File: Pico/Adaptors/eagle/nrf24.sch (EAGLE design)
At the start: 3 parts

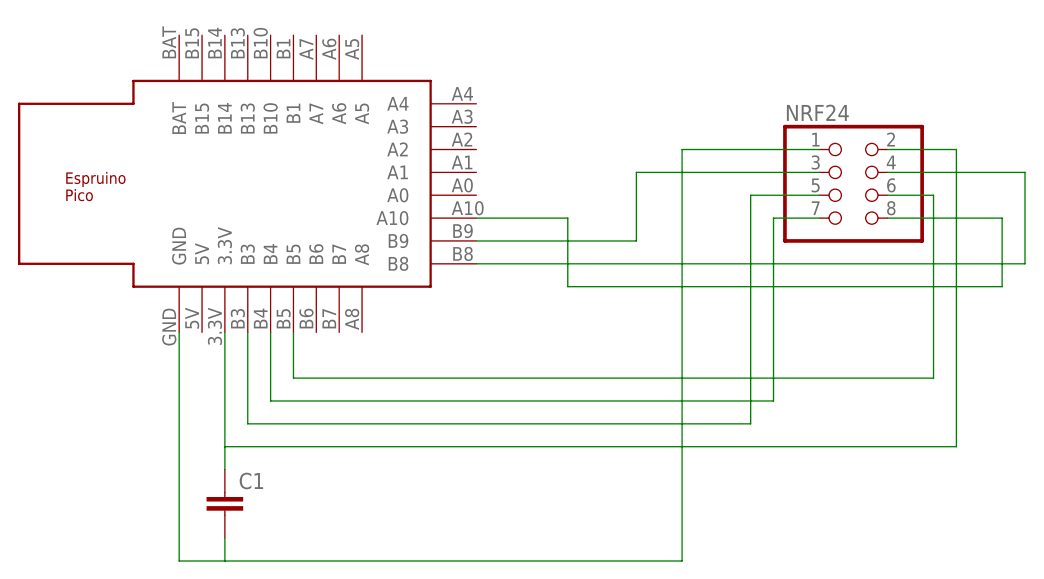
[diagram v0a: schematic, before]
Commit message: updated NRF24, new Pico library part that does 0.1 holes and 0.05 SMD
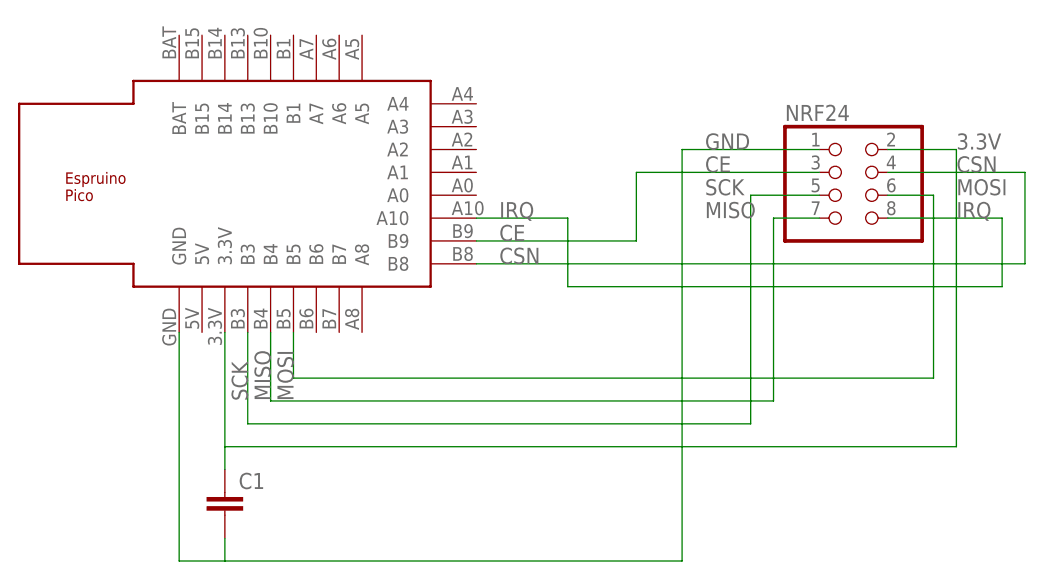
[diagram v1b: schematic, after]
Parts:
- removed U$1: ESPRUINO_PICO_SMDONLY, espruino_pico:ESPRUINO_PICO_SMDONLY
- added U$2: ESPRUINO_PICO_HALFSMD, espruino_pico:ESPRUINO_PICO_HALFSMD
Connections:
- removed net N$1: C1.1, NRF24.2, U$1.3.3V
- removed net N$2: C1.2, NRF24.1, U$1.GND
- removed net N$4: NRF24.5, U$1.B3
- removed net N$5: NRF24.7, U$1.B4
- removed net N$6: NRF24.6, U$1.B5
- removed net N$7: NRF24.4, U$1.B8
- removed net N$8: NRF24.3, U$1.B9
- removed net N$9: NRF24.8, U$1.A10
- new net 3.3V: C1.1, NRF24.2, U$2.3.3V
- new net CE: NRF24.3, U$2.B9
- new net CSN: NRF24.4, U$2.B8
- new net GND: C1.2, NRF24.1, U$2.GND
- new net IRQ: NRF24.8, U$2.A10
- new net MISO: NRF24.7, U$2.B4
- new net MOSI: NRF24.6, U$2.B5
- new net SCK: NRF24.5, U$2.B3
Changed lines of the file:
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@@
 <grid distance="0.1" unitdist="inch" unit="inch" style="lines" multiple="1" display="no" altdistance="0.01" altunitdist="inch" altunit="inch"/>
 <layers>
-<layer number="1" name="Top" color="4" fill="1" visible="no" active="no"/>
-<layer number="16" name="Bottom" color="1" fill="1" visible="no" active="no"/>
-<layer number="17" name="Pads" color="2" fill="1" visible="no" active="no"/>
-<layer number="18" name="Vias" color="2" fill="1" visible="no" active="no"/>
-<layer number="19" name="Unrouted" color="6" fill="1" visible="no" active="no"/>
-<layer number="20" name="Dimension" color="15" fill="1" visible="no" active="no"/>
-<layer number="21" name="tPlace" color="7" fill="1" visible="no" active="no"/>
-<layer number="22" name="bPlace" color="7" fill="1" visible="no" active="no"/>
-<layer number="23" name="tOrigins" color="15" fill="1" visible="no" active="no"/>
-<layer number="24" name="bOrigins" color="15" fill="1" visible="no" active="no"/>
-<layer number="25" name="tNames" color="7" fill="1" visible="no" active="no"/>
-<layer number="26" name="bNames" color="7" fill="1" visible="no" active="no"/>
-<layer number="27" name="tValues" color="7" fill="1" visible="no" active="no"/>
-<layer number="28" name="bValues" color="7" fill="1" visible="no" active="no"/>
+<layer number="1" name="Top" color="4" fill="1" visible="yes" active="no"/>
+<layer number="16" name="Bottom" color="1" fill="1" visible="yes" active="no"/>
+<layer number="17" name="Pads" color="2" fill="1" visible="yes" active="no"/>
+<layer number="18" name="Vias" color="2" fill="1" visible="yes" active="no"/>
+<layer number="19" name="Unrouted" color="6" fill="1" visible="yes" active="no"/>
+<layer number="20" name="Dimension" color="15" fill="1" visible="yes" active="no"/>
+<layer number="21" name="tPlace" color="7" fill="1" visible="yes" active="no"/>
+<layer number="22" name="bPlace" color="7" fill="1" visible="yes" active="no"/>
+<layer number="23" name="tOrigins" color="15" fill="1" visible="yes" active="no"/>
+<layer number="24" name="bOrigins" color="15" fill="1" visible="yes" active="no"/>
+<layer number="25" name="tNames" color="7" fill="1" visible="yes" active="no"/>
+<layer number="26" name="bNames" color="7" fill="1" visible="yes" active="no"/>
+<layer number="27" name="tValues" color="7" fill="1" visible="yes" active="no"/>
+<layer number="28" name="bValues" color="7" fill="1" visible="yes" active="no"/>
 <layer number="29" name="tStop" color="7" fill="3" visible="no" active="no"/>
 <layer number="30" name="bStop" color="7" fill="6" visible="no" active="no"/>
@@
 <layer number="35" name="tGlue" color="7" fill="4" visible="no" active="no"/>
 <layer number="36" name="bGlue" color="7" fill="5" visible="no" active="no"/>
-<layer number="37" name="tTest" color="7" fill="1" visible="no" active="no"/>
-<layer number="38" name="bTest" color="7" fill="1" visible="no" active="no"/>
+<layer number="37" name="tTest" color="7" fill="1" visible="yes" active="no"/>
+<layer number="38" name="bTest" color="7" fill="1" visible="yes" active="no"/>
 <layer number="39" name="tKeepout" color="4" fill="11" visible="no" active="no"/>
 <layer number="40" name="bKeepout" color="1" fill="11" visible="no" active="no"/>
@@
 <layer number="44" name="Drills" color="7" fill="1" visible="no" active="no"/>
 <layer number="45" name="Holes" color="7" fill="1" visible="no" active="no"/>
-<layer number="46" name="Milling" color="3" fill="1" visible="no" active="no"/>
-<layer number="47" name="Measures" color="7" fill="1" visible="no" active="no"/>
-<layer number="48" name="Document" color="7" fill="1" visible="no" active="no"/>
-<layer number="49" name="Reference" color="7" fill="1" visible="no" active="no"/>
-<layer number="51" name="tDocu" color="7" fill="1" visible="no" active="no"/>
-<layer number="52" name="bDocu" color="7" fill="1" visible="no" active="no"/>
+<layer number="46" name="Milling" color="3" fill="1" visible="yes" active="no"/>
+<layer number="47" name="Measures" color="7" fill="1" visible="yes" active="no"/>
+<layer number="48" name="Document" color="7" fill="1" visible="yes" active="no"/>
+<layer number="49" name="Reference" color="7" fill="1" visible="yes" active="no"/>
+<layer number="51" name="tDocu" color="7" fill="1" visible="yes" active="no"/>
+<layer number="52" name="bDocu" color="7" fill="1" visible="yes" active="no"/>
 <layer number="91" name="Nets" color="2" fill="1" visible="yes" active="yes"/>
 <layer number="92" name="Busses" color="1" fill="1" visible="yes" active="yes"/>
@@
 <part name="NRF24" library="pinhead" deviceset="PINHD-2X4" device=""/>
 <part name="C1" library="rcl" deviceset="C-EU" device="C1206"/>
-<part name="U$1" library="espruino_pico" deviceset="ESPRUINO_PICO_SMDONLY" device=""/>
+<part name="U$2" library="espruino_pico" deviceset="ESPRUINO_PICO_HALFSMD" device=""/>
 </parts>
 <sheets>
@@
 <instance part="NRF24" gate="A" x="99.06" y="55.88"/>
 <instance part="C1" gate="G$1" x="30.48" y="22.86"/>
-<instance part="U$1" gate="G$1" x="33.02" y="66.04"/>
+<instance part="U$2" gate="G$1" x="33.02" y="66.04"/>
 </instances>
 <busses>
 </busses>
 <nets>
-<net name="N$1" class="0">
+<net name="3.3V" class="0">
 <segment>
 <pinref part="C1" gate="G$1" pin="1"/>
@@
 <wire x1="111.76" y1="60.96" x2="111.76" y2="27.94" width="0.1524" layer="91"/>
 <wire x1="111.76" y1="27.94" x2="30.48" y2="27.94" width="0.1524" layer="91"/>
-<pinref part="U$1" gate="G$1" pin="3.3V"/>
+<label x="111.76" y="60.96" size="1.778" layer="95"/>
+<pinref part="U$2" gate="G$1" pin="3.3V"/>
 </segment>
 </net>
-<net name="N$2" class="0">
+<net name="GND" class="0">
 <segment>
 <wire x1="25.4" y1="40.64" x2="25.4" y2="15.24" width="0.1524" layer="91"/>
@@
 <pinref part="NRF24" gate="A" pin="1"/>
 <wire x1="81.28" y1="60.96" x2="96.52" y2="60.96" width="0.1524" layer="91"/>
-<pinref part="U$1" gate="G$1" pin="GND"/>
+<label x="83.82" y="60.96" size="1.778" layer="95"/>
+<pinref part="U$2" gate="G$1" pin="GND"/>
 </segment>
 </net>
-<net name="N$4" class="0">
+<net name="SCK" class="0">
 <segment>
 <wire x1="33.02" y1="40.64" x2="33.02" y2="30.48" width="0.1524" layer="91"/>
@@
 <pinref part="NRF24" gate="A" pin="5"/>
 <wire x1="88.9" y1="55.88" x2="96.52" y2="55.88" width="0.1524" layer="91"/>
-<pinref part="U$1" gate="G$1" pin="B3"/>
+<label x="83.82" y="55.88" size="1.778" layer="95"/>
+<label x="33.02" y="33.02" size="1.778" layer="95" rot="R90"/>
+<pinref part="U$2" gate="G$1" pin="B3"/>
 </segment>
 </net>
-<net name="N$5" class="0">
+<net name="MISO" class="0">
 <segment>
 <pinref part="NRF24" gate="A" pin="7"/>
@@
 <wire x1="91.44" y1="33.02" x2="35.56" y2="33.02" width="0.1524" layer="91"/>
 <wire x1="35.56" y1="33.02" x2="35.56" y2="40.64" width="0.1524" layer="91"/>
-<pinref part="U$1" gate="G$1" pin="B4"/>
+<label x="83.82" y="53.34" size="1.778" layer="95"/>
+<label x="35.56" y="33.02" size="1.778" layer="95" rot="R90"/>
+<pinref part="U$2" gate="G$1" pin="B4"/>
 </segment>
 </net>
-<net name="N$6" class="0">
+<net name="MOSI" class="0">
 <segment>
 <wire x1="38.1" y1="40.64" x2="38.1" y2="35.56" width="0.1524" layer="91"/>
@@
 <pinref part="NRF24" gate="A" pin="6"/>
 <wire x1="109.22" y1="55.88" x2="104.14" y2="55.88" width="0.1524" layer="91"/>
-<pinref part="U$1" gate="G$1" pin="B5"/>
+<label x="111.76" y="55.88" size="1.778" layer="95"/>
+<label x="38.1" y="33.02" size="1.778" layer="95" rot="R90"/>
+<pinref part="U$2" gate="G$1" pin="B5"/>
 </segment>
 </net>
-<net name="N$7" class="0">
+<net name="CSN" class="0">
 <segment>
 <wire x1="58.42" y1="48.26" x2="119.38" y2="48.26" width="0.1524" layer="91"/>
@@
 <pinref part="NRF24" gate="A" pin="4"/>
 <wire x1="119.38" y1="58.42" x2="104.14" y2="58.42" width="0.1524" layer="91"/>
-<pinref part="U$1" gate="G$1" pin="B8"/>
+<label x="111.76" y="58.42" size="1.778" layer="95"/>
+<label x="60.96" y="48.26" size="1.778" layer="95"/>
+<pinref part="U$2" gate="G$1" pin="B8"/>
 </segment>
 </net>
-<net name="N$8" class="0">
+<net name="CE" class="0">
 <segment>
 <pinref part="NRF24" gate="A" pin="3"/>
@@
 <wire x1="76.2" y1="58.42" x2="76.2" y2="50.8" width="0.1524" layer="91"/>
 <wire x1="76.2" y1="50.8" x2="58.42" y2="50.8" width="0.1524" layer="91"/>
-<pinref part="U$1" gate="G$1" pin="B9"/>
+<label x="83.82" y="58.42" size="1.778" layer="95"/>
+<label x="60.96" y="50.8" size="1.778" layer="95"/>
+<pinref part="U$2" gate="G$1" pin="B9"/>
 </segment>
 </net>
-<net name="N$9" class="0">
+<net name="IRQ" class="0">
 <segment>
 <wire x1="58.42" y1="53.34" x2="68.58" y2="53.34" width="0.1524" layer="91"/>
@@
 <pinref part="NRF24" gate="A" pin="8"/>
 <wire x1="116.84" y1="53.34" x2="104.14" y2="53.34" width="0.1524" layer="91"/>
-<pinref part="U$1" gate="G$1" pin="A10"/>
+<label x="111.76" y="53.34" size="1.778" layer="95"/>
+<label x="60.96" y="53.34" size="1.778" layer="95"/>
+<pinref part="U$2" gate="G$1" pin="A10"/>
 </segment>
 </net>
